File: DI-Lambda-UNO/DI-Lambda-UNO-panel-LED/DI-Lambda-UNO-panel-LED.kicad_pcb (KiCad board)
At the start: 2 copper layers, 33.2 x 26.6 mm, 6 parts, among them J1 Conn_01X06, U1 24LC02

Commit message: DI-Lambda UNO LED module cleanup
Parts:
- J1: footprint Sprint-contact-connector-2:Contact-2.5x6 -> Spring-contact-connector-2:Contact-2.5x6
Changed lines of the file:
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@@
     )
   )
-  (module Sprint-contact-connector-2:Contact-2.5x6 (layer F.Cu)
+  (module Spring-contact-connector-2:Contact-2.5x6 (layer F.Cu)
     (at 160 90.7)
     (fp_text reference J1 (at -9 -2.4) (layer F.SilkS) hide

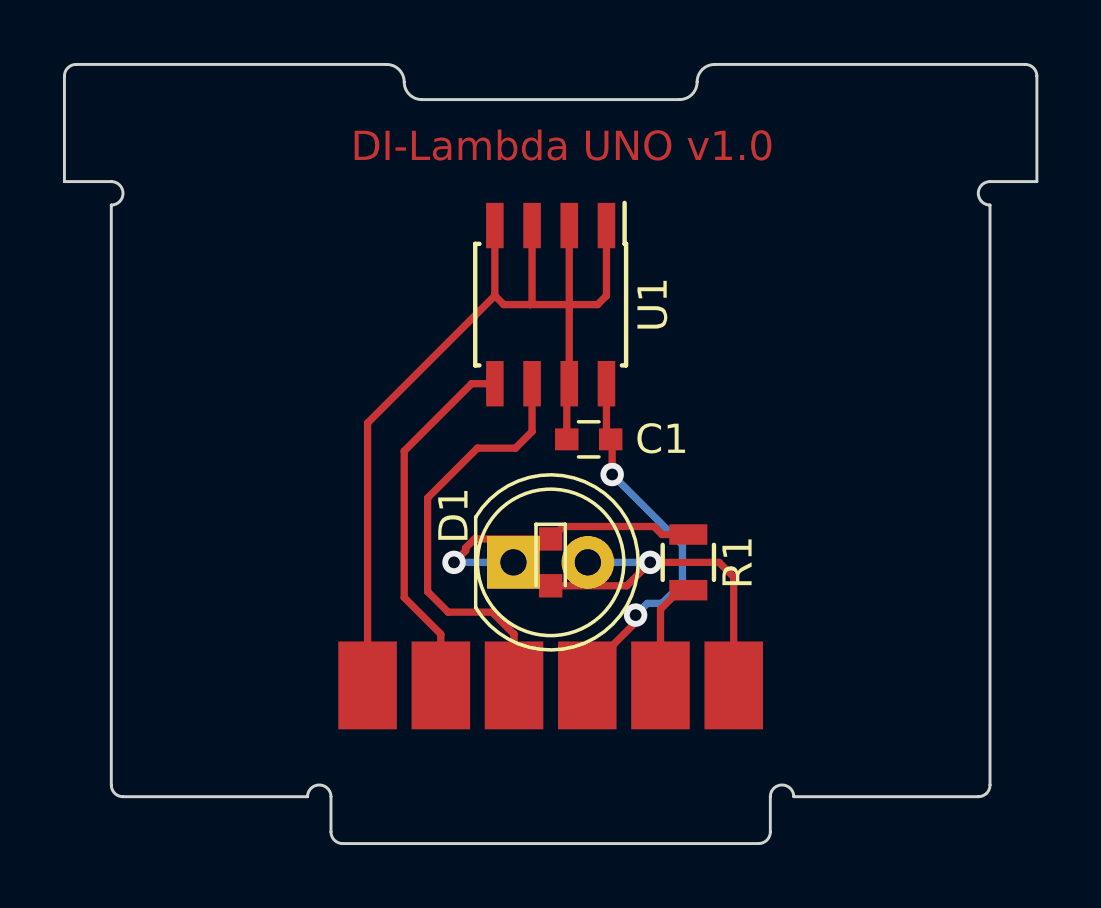
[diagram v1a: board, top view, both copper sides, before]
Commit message: Use longer contact pas for the spring connector
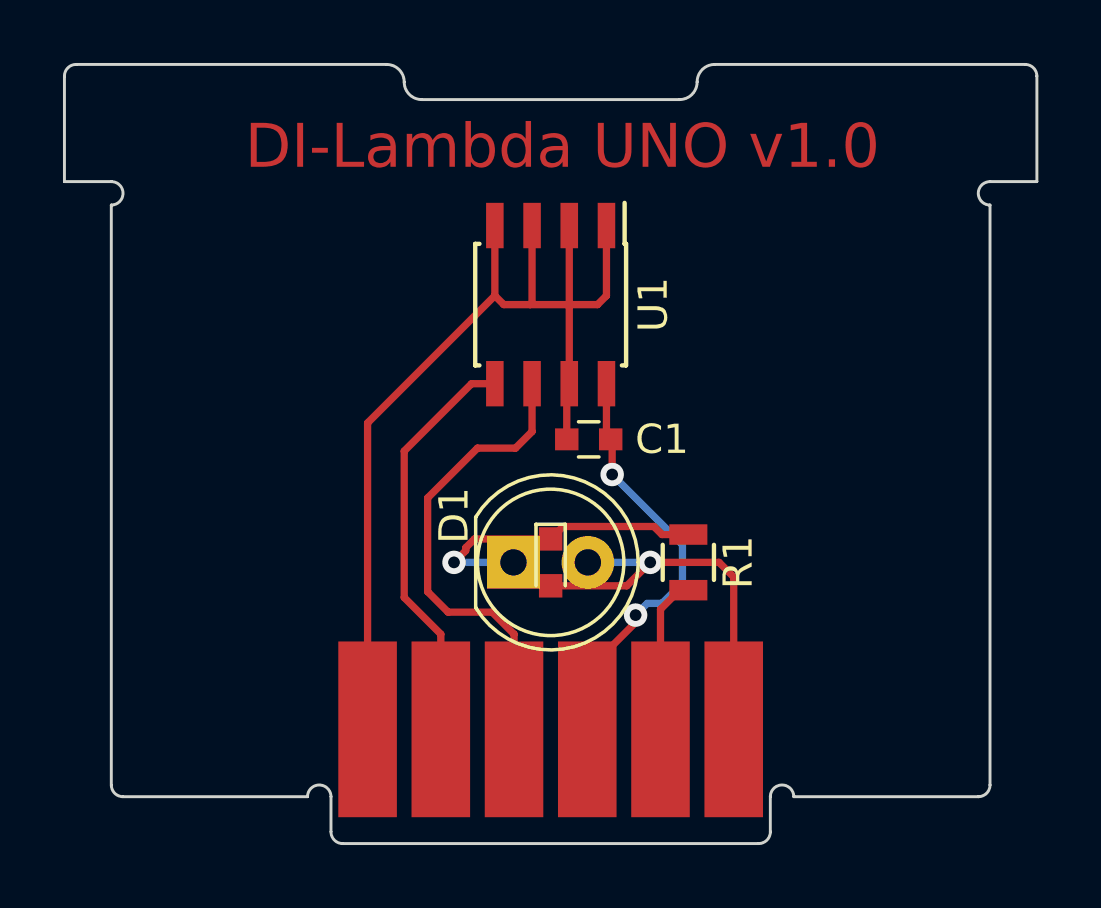
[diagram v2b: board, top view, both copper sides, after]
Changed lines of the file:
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@@
-(kicad_pcb (version 20170123) (host pcbnew "(2017-07-27 revision 3ee2f80)-test1")
+(kicad_pcb (version 20170123) (host pcbnew "(2017-09-07 revision 3b08636)-master")
   (general
     (thickness 1.6)
@@
       (layerselection 0x000f0_ffffffff)
       (usegerberextensions true)
+      (usegerberattributes true)
+      (usegerberadvancedattributes true)
+      (creategerberjobfile true)
       (excludeedgelayer false)
       (linewidth 0.100000)
@@
     (add_net "Net-(D1-Pad1)")
   )
+  (module Spring-contact-connector-2:Contact-2.5x6 (layer F.Cu)
+    (at 160 90.7)
+    (fp_text reference J1 (at -9 -2.4) (layer F.SilkS) hide
+      (effects (font (size 1 1) (thickness 0.15)))
+    )
+    (fp_text value Conn_01X06 (at 0 1.5) (layer F.Fab)
+      (effects (font (size 1 1) (thickness 0.15)))
+    )
+    (pad 6 smd rect (at 6.25 -1) (size 2 6) (layers F.Cu F.Paste F.Mask)
+      (net 6 /VLED))
+    (pad 5 smd rect (at 3.75 -1) (size 2 6) (layers F.Cu F.Paste F.Mask)
+      (net 5 /GLED))
+    (pad 4 smd rect (at 1.25 -1) (size 2 6) (layers F.Cu F.Paste F.Mask)
+      (net 4 /VCC))
+    (pad 3 smd rect (at -1.25 -1) (size 2 6) (layers F.Cu F.Paste F.Mask)
+      (net 3 /SCL))
+    (pad 2 smd rect (at -3.75 -1) (size 2 6) (layers F.Cu F.Paste F.Mask)
+      (net 2 /SDA))
+    (pad 1 smd rect (at -6.25 -1) (size 2 6) (layers F.Cu F.Paste F.Mask)
+      (net 1 GND))
+  )
   (module LED-single-layer:LED_D5.0mm (layer F.Cu)
     (at 158.73 84)
@@
       (rotate (xyz 0 0 0))
     )
-  )
-  (module Spring-contact-connector-2:Contact-2.5x6 (layer F.Cu)
-    (at 160 90.7)
-    (fp_text reference J1 (at -9 -2.4) (layer F.SilkS) hide
-      (effects (font (size 1 1) (thickness 0.15)))
-    )
-    (fp_text value Conn_01X06 (at 0 1.5) (layer F.Fab)
-      (effects (font (size 1 1) (thickness 0.15)))
-    )
-    (pad 6 smd rect (at 6.25 -2.5) (size 2 3) (layers F.Cu F.Paste F.Mask)
-      (net 6 /VLED))
-    (pad 5 smd rect (at 3.75 -2.5) (size 2 3) (layers F.Cu F.Paste F.Mask)
-      (net 5 /GLED))
-    (pad 4 smd rect (at 1.25 -2.5) (size 2 3) (layers F.Cu F.Paste F.Mask)
-      (net 4 /VCC))
-    (pad 3 smd rect (at -1.25 -2.5) (size 2 3) (layers F.Cu F.Paste F.Mask)
-      (net 3 /SCL))
-    (pad 2 smd rect (at -3.75 -2.5) (size 2 3) (layers F.Cu F.Paste F.Mask)
-      (net 2 /SDA))
-    (pad 1 smd rect (at -6.25 -2.5) (size 2 3) (layers F.Cu F.Paste F.Mask)
-      (net 1 GND))
   )
   (module Capacitors_SMD:C_0603 (layer F.Cu)
@@
   )
   (gr_text "DI-Lambda UNO v1.0" (at 160.4 69.8) (layer F.Cu)
-    (effects (font (size 1 1) (thickness 0.2)))
+    (effects (font (size 1.5 1.5) (thickness 0.3)))
   )
   (dimension 4 (width 0.3) (layer Eco1.User)

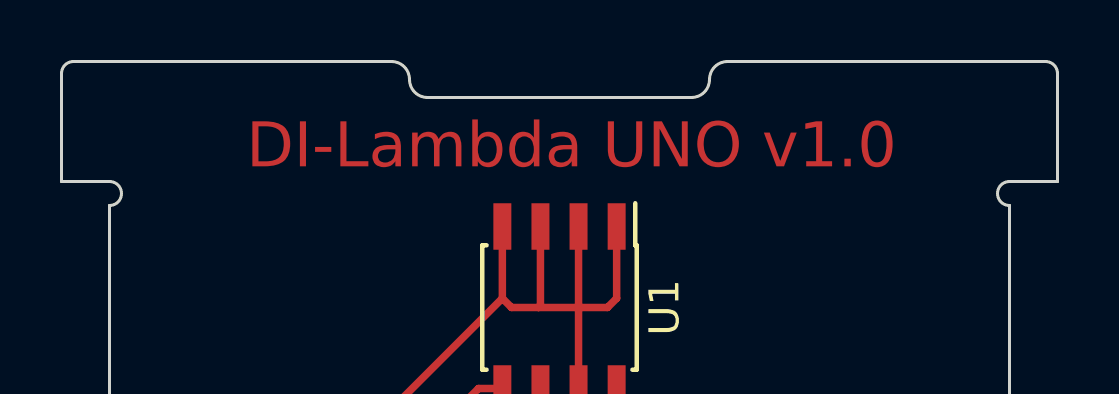
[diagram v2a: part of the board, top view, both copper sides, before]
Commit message: Remove notches from the LED/Sensor/Pinhole panels
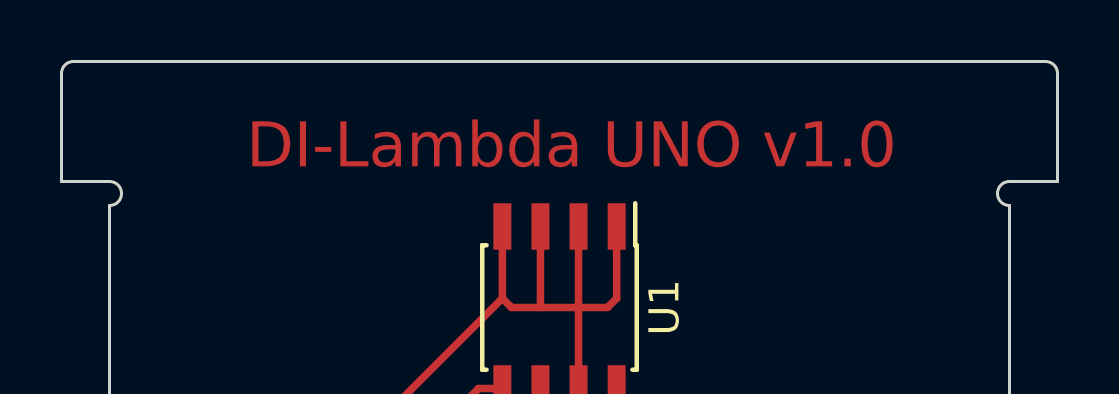
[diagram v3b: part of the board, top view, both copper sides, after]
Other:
- outline, holes or cut-outs redrawn
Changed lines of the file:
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@@
   (general
     (thickness 1.6)
-    (drawings 32)
+    (drawings 26)
     (tracks 64)
     (zones 0)
@@
   (gr_arc (start 167.9 92) (end 167.5 92) (angle 180) (layer Edge.Cuts) (width 0.1))
   (gr_arc (start 152.1 92) (end 151.7 92) (angle 180) (layer Edge.Cuts) (width 0.1))
-  (gr_arc (start 164.4 67.6) (end 165 67.6) (angle 90) (layer Edge.Cuts) (width 0.1))
-  (gr_arc (start 165.6 67.6) (end 165 67.6) (angle 90) (layer Edge.Cuts) (width 0.1))
-  (gr_arc (start 154.4 67.6) (end 154.4 67) (angle 90) (layer Edge.Cuts) (width 0.1))
-  (gr_arc (start 155.6 67.6) (end 155.6 68.2) (angle 90) (layer Edge.Cuts) (width 0.1))
   (gr_line (start 175 91.6) (end 175 71.8) (layer Edge.Cuts) (width 0.1))
-  (gr_line (start 154.4 67) (end 143.8 67) (layer Edge.Cuts) (width 0.1))
+  (gr_line (start 176.2 67) (end 143.8 67) (layer Edge.Cuts) (width 0.1))
   (gr_line (start 175 71) (end 176.6 71) (layer Edge.Cuts) (width 0.1))
   (gr_line (start 145 91.6) (end 145 71.8) (layer Edge.Cuts) (width 0.1))
@@
   (gr_line (start 152.5 92) (end 152.5 93.2) (layer Edge.Cuts) (width 0.1))
   (gr_line (start 145.4 92) (end 151.7 92) (layer Edge.Cuts) (width 0.1))
-  (gr_line (start 176.2 67) (end 165.6 67) (layer Edge.Cuts) (width 0.1))
-  (gr_line (start 155.6 68.2) (end 164.4 68.2) (layer Edge.Cuts) (width 0.1))
   (segment (start 153.75 88.2) (end 153.75 79.24) (width 0.25) (layer F.Cu) (net 1))
   (segment (start 153.75 79.24) (end 158.095 74.895) (width 0.25) (layer F.Cu) (net 1))

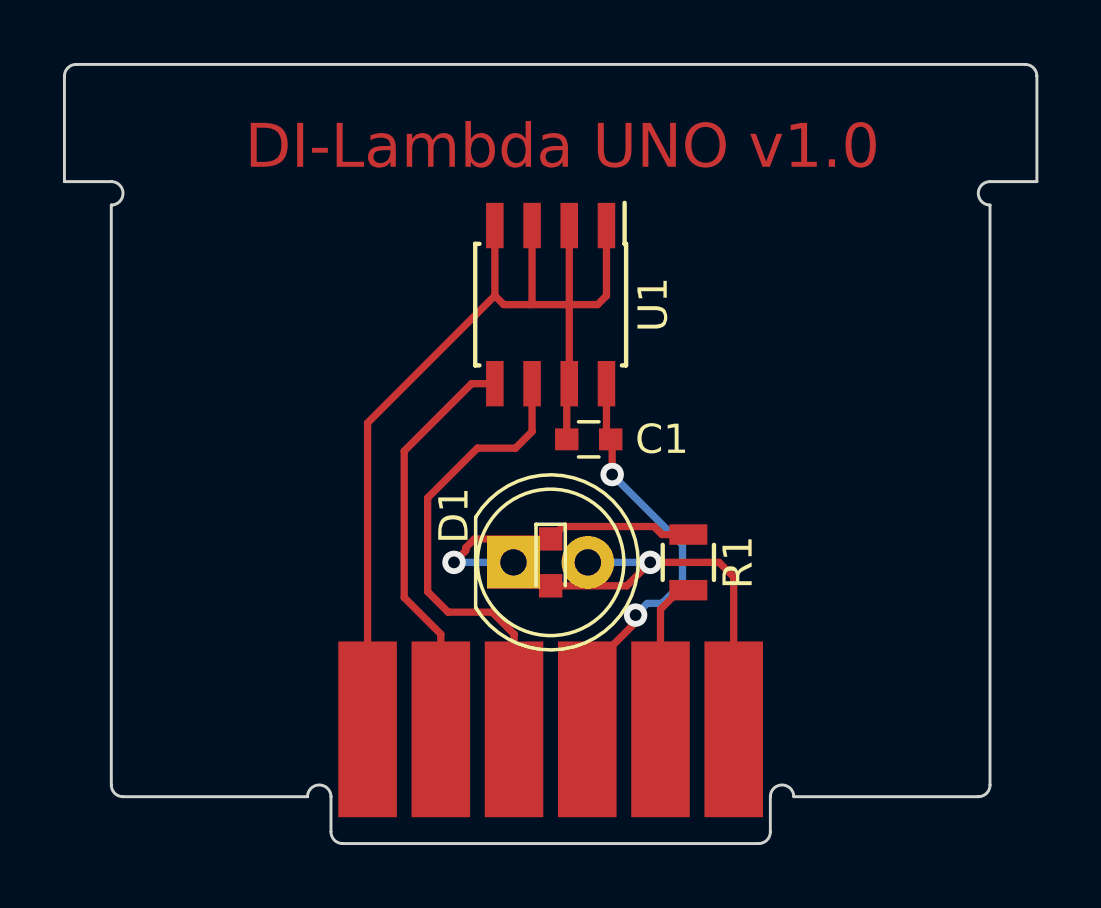
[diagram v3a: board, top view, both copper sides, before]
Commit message: Copper pour on the LED board
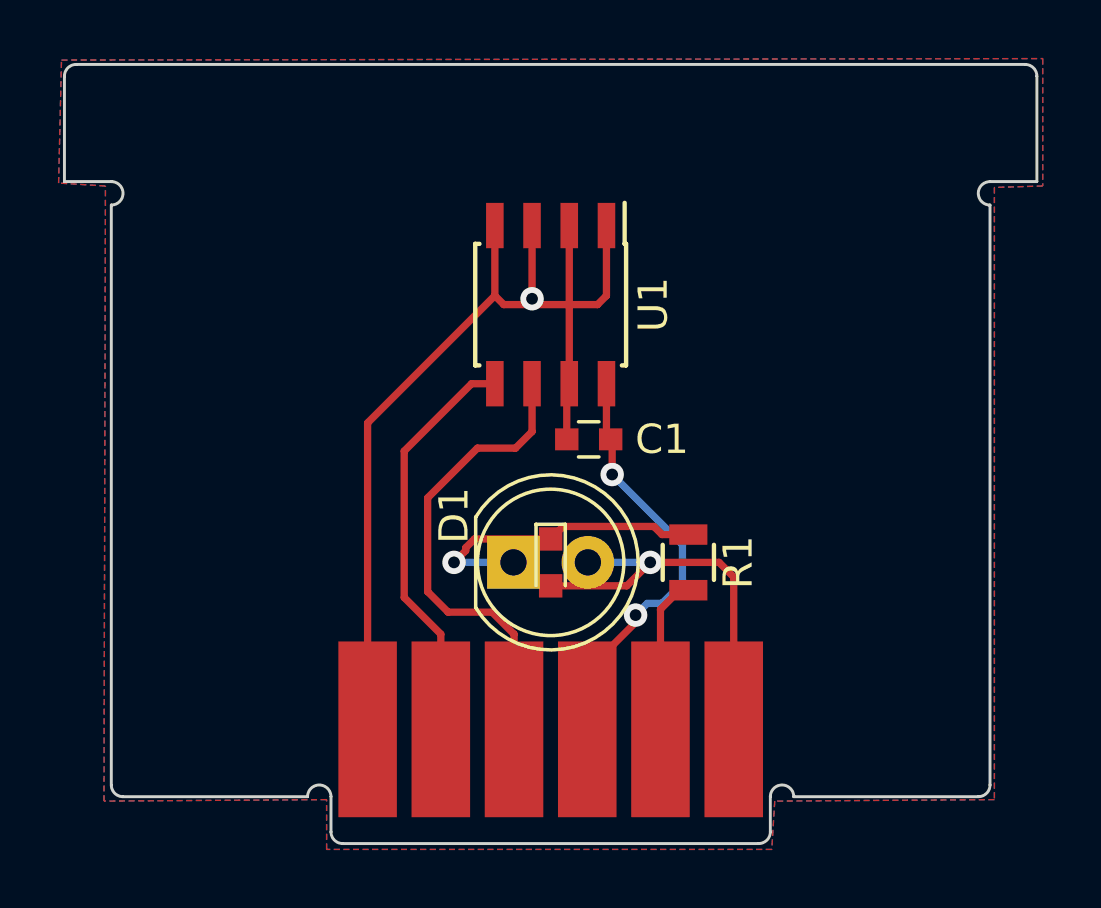
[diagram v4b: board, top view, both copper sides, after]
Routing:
- net GND: vias 0 -> 1
- added copper zone on B.Cu, net GND
- added copper zone on F.Cu, net GND
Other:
- board text added: "DI-Lambda UNO v1.1"
- board text removed: "DI-Lambda UNO v1.0"
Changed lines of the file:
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@@
     (thickness 1.6)
     (drawings 26)
-    (tracks 64)
+    (tracks 66)
     (zones 0)
     (modules 6)
@@
     (40 Dwgs.User user)
     (41 Cmts.User user)
-    (42 Eco1.User user)
+    (42 Eco1.User user hide)
     (43 Eco2.User user)
     (44 Edge.Cuts user)
@@
     )
   )
-  (gr_text "DI-Lambda UNO v1.0" (at 160.4 69.8) (layer F.Cu)
+  (gr_text "DI-Lambda UNO v1.1" (at 160.4 69.8) (layer F.Mask)
     (effects (font (size 1.5 1.5) (thickness 0.3)))
   )
@@
   (gr_line (start 152.5 92) (end 152.5 93.2) (layer Edge.Cuts) (width 0.1))
   (gr_line (start 145.4 92) (end 151.7 92) (layer Edge.Cuts) (width 0.1))
+  (segment (start 159.365 75) (end 159.365 75.135) (width 0.25) (layer F.Cu) (net 1))
+  (segment (start 159.365 72.5) (end 159.365 75) (width 0.25) (layer F.Cu) (net 1))
+  (via (at 159.365 75) (size 0.8) (drill 0.4) (layers F.Cu B.Cu) (net 1))
   (segment (start 153.75 88.2) (end 153.75 79.24) (width 0.25) (layer F.Cu) (net 1))
   (segment (start 153.75 79.24) (end 158.095 74.895) (width 0.25) (layer F.Cu) (net 1))
@@
   (segment (start 158.4 75.2) (end 159.3 75.2) (width 0.25) (layer F.Cu) (net 1))
   (segment (start 159.365 75.135) (end 159.3 75.2) (width 0.25) (layer F.Cu) (net 1))
-  (segment (start 159.365 72.5) (end 159.365 75.135) (width 0.25) (layer F.Cu) (net 1))
   (segment (start 161.6 75.2) (end 161.905 74.895) (width 0.25) (layer F.Cu) (net 1))
   (segment (start 161.905 74.895) (end 161.905 72.5) (width 0.25) (layer F.Cu) (net 1))
@@
   (segment (start 158.73 84) (end 156.7 84) (width 0.25) (layer B.Cu) (net 7))
   (via (at 156.7 84) (size 0.8) (drill 0.4) (layers F.Cu B.Cu) (net 7))
+  (zone (net 1) (net_name GND) (layer F.Cu) (hatch edge 0.508)
+    (connect_pads (clearance 0.508))
+    (min_thickness 0.254)
+    (fill yes (arc_segments 16) (thermal_gap 0.508) (thermal_bridge_width 0.508))
+    (polygon
+      (pts
+        (xy 143.3 66.85) (xy 176.8 66.8) (xy 176.8 71.15) (xy 175.15 71.2) (xy 175.15 92.1)
+        (xy 167.65 92.15) (xy 167.55 93.8) (xy 152.35 93.8) (xy 152.35 92.1) (xy 144.75 92.15)
+        (xy 144.8 71.15) (xy 143.2 71.05)
+      )
+    )
+  )
+  (zone (net 1) (net_name GND) (layer B.Cu) (hatch edge 0.508)
+    (connect_pads (clearance 0.508))
+    (min_thickness 0.254)
+    (fill yes (arc_segments 16) (thermal_gap 0.508) (thermal_bridge_width 0.508))
+    (polygon
+      (pts
+        (xy 143.3 66.85) (xy 176.8 66.8) (xy 176.8 71.15) (xy 175.15 71.2) (xy 175.15 92.1)
+        (xy 167.65 92.15) (xy 167.55 93.8) (xy 152.35 93.8) (xy 152.35 92.1) (xy 144.75 92.15)
+        (xy 144.8 71.15) (xy 143.2 71.05)
+      )
+    )
+  )
 )
